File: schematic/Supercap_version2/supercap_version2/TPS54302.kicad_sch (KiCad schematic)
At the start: 12 parts, among them SW3 SW_DIP_x01, U2 TPS54302

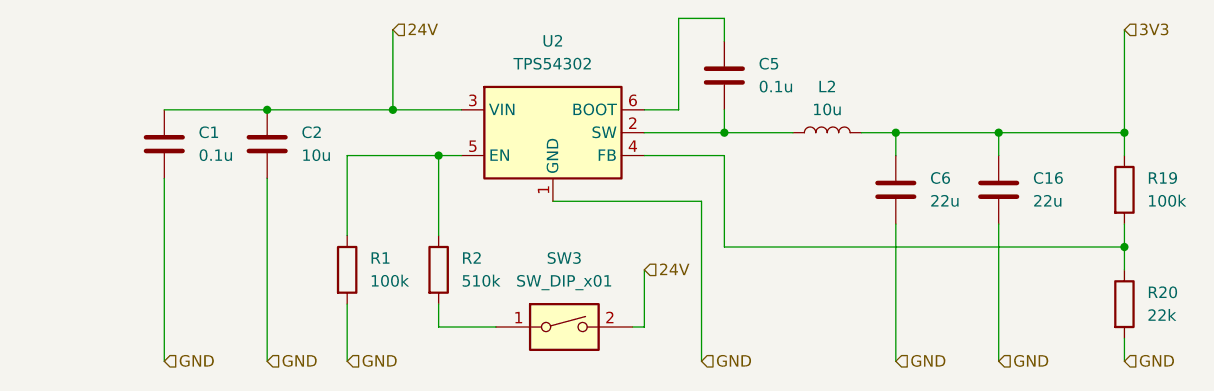
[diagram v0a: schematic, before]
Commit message: TODO: PA5 - hard safe mode check Added hard safe mode via blocking soft safe mode, reed switch added
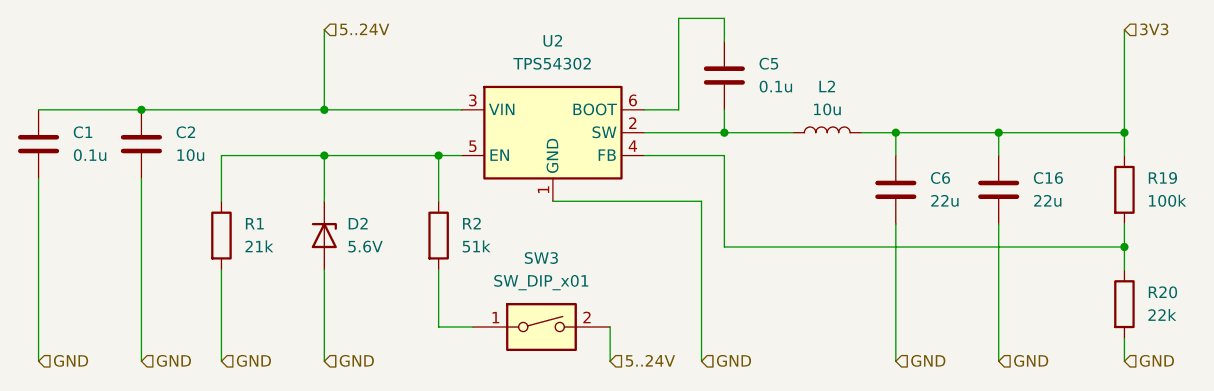
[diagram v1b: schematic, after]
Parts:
- added D2: 5.6V, symbol Device:D_Zener
- R1: value 100k -> 21k
- R2: value 510k -> 51k
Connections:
- net GND: now also D2.2 (A)
- net at R1.1, R2.1, U2.5 (EN): now also D2.1 (K)
- net 24V renamed 5..24V
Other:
- moved on the sheet: C1, C2, R1, R2, SW3

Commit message: Updated board + PA5 hard safe mode (unchecked)
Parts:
- D2: value 5.6V -> 3.3V
- R1: value 21k -> 10k
- R2: value 51k -> 20k
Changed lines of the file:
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@@
 			)
 		)
-		(property "Value" "5.6V"
+		(property "Value" "3.3V"
 			(at 110.49 106.6799 90)
 			(effects
@@
 			)
 		)
-		(property "Value" "51k"
+		(property "Value" "20k"
 			(at 123.19 106.6799 0)
 			(effects
@@
 			)
 		)
-		(property "Value" "21k"
+		(property "Value" "10k"
 			(at 99.06 106.6799 0)
 			(effects
